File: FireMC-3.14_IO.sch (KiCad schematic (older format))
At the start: 2 parts

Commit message: Schematic Update and Design Calcs for 3V3
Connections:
- net labels removed: +3V3
- wire segments 45 -> 42
- no-connect marks 4 -> 6
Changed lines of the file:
@@
 Connection ~ 2800 2100
-Wire Wire Line
-	2000 2300 1800 2300
-Wire Wire Line
-	1800 2300 1800 1400
-Connection ~ 1800 1500
 Wire Wire Line
 	2000 1900 1900 1900
@@
 	2700 2600 3300 2600
 $Comp
-L GND #PWR?
+L GND #PWR021
 U 1 1 57CB4DBD
 P 1900 3500
-F 0 "#PWR?" H 1900 3250 50  0001 C CNN
+F 0 "#PWR021" H 1900 3250 50  0001 C CNN
 F 1 "GND" H 1900 3350 50  0000 C CNN
 F 2 "" H 1900 3500 50  0000 C CNN
@@
 $EndComp
 $Comp
-L GND #PWR?
+L GND #PWR022
 U 1 1 57CB4DD3
 P 2800 3500
-F 0 "#PWR?" H 2800 3250 50  0001 C CNN
+F 0 "#PWR022" H 2800 3250 50  0001 C CNN
 F 1 "GND" H 2800 3350 50  0000 C CNN
 F 2 "" H 2800 3500 50  0000 C CNN
 F 3 "" H 2800 3500 50  0000 C CNN
 	1    2800 3500
-	1    0    0    -1
-$EndComp
-$Comp
-L +3V3 #PWR?
-U 1 1 57CB4DE9
-P 1800 1400
-F 0 "#PWR?" H 1800 1250 50  0001 C CNN
-F 1 "+3V3" H 1800 1540 50  0000 C CNN
-F 2 "" H 1800 1400 50  0000 C CNN
-F 3 "" H 1800 1400 50  0000 C CNN
-	1    1800 1400
 	1    0    0    -1
 $EndComp
@@
 $EndComp
 $Comp
-L GND #PWR?
+L GND #PWR024
 U 1 1 57CB72B4
 P 4950 1600
-F 0 "#PWR?" H 4950 1350 50  0001 C CNN
+F 0 "#PWR024" H 4950 1350 50  0001 C CNN
 F 1 "GND" H 4950 1450 50  0000 C CNN
 F 2 "" H 4950 1600 50  0000 C CNN
@@
 $EndComp
 $Comp
-L +5F #PWR?
+L +5F #PWR025
 U 1 1 57CB7400
 P 4950 900
-F 0 "#PWR?" H 4950 750 50  0001 C CNN
+F 0 "#PWR025" H 4950 750 50  0001 C CNN
 F 1 "+5F" H 4950 1040 50  0000 C CNN
 F 2 "" H 4950 900 50  0000 C CNN
@@
 $EndComp
 $Comp
-L +5V #PWR?
+L +5V #PWR026
 U 1 1 57CB7418
 P 3850 900
-F 0 "#PWR?" H 3850 750 50  0001 C CNN
+F 0 "#PWR026" H 3850 750 50  0001 C CNN
 F 1 "+5V" H 3850 1040 50  0000 C CNN
 F 2 "" H 3850 900 50  0000 C CNN
@@
 Wire Wire Line
 	4950 1100 5150 1100
-Wire Wire Line
-	1800 1500 2000 1500
 Text GLabel 1400 1600 0    50   Input ~ 0
 SDA1
@@
 Text GLabel 3300 3400 2    50   Input ~ 0
 GPIO21
+NoConn ~ 2000 2300
+NoConn ~ 2000 1500
 $EndSCHEMATC

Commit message: math check
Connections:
- net labels removed: +5F
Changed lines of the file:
@@
 $EndComp
 $Comp
-L +5F #PWR025
-U 1 1 57CB7400
+L +5V #PWR026
+U 1 1 57CB7418
 P 4950 900
-F 0 "#PWR025" H 4950 750 50  0001 C CNN
-F 1 "+5F" H 4950 1040 50  0000 C CNN
+F 0 "#PWR026" H 4950 750 50  0001 C CNN
+F 1 "+5V" H 4950 1040 50  0000 C CNN
 F 2 "" H 4950 900 50  0000 C CNN
 F 3 "" H 4950 900 50  0000 C CNN
@@
 	1    0    0    -1
 $EndComp
-$Comp
-L +5V #PWR026
-U 1 1 57CB7418
-P 3850 900
-F 0 "#PWR026" H 3850 750 50  0001 C CNN
-F 1 "+5V" H 3850 1040 50  0000 C CNN
-F 2 "" H 3850 900 50  0000 C CNN
-F 3 "" H 3850 900 50  0000 C CNN
-	1    3850 900
-	1    0    0    -1
-$EndComp

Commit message: Schematic 80% complete
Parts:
- added J? (x3): Header_1X2, symbol Header_1X2
- added J? (x4): Header_1X3, symbol Header_1X3
- added Q? (x3): Q_PMOS_GDS, symbol Q_PMOS_GDS
- added R? (x2): 3k3, symbol R
- added U?: MCP23S17, symbol MCP23S17
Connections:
- net GND: now also J?.2, J?.2, J?.2, J?.2, Q?.3 (S), Q?.3 (S), Q?.3 (S), U?.10 (VSS), U?.15 (A0), U?.16 (A1), U?.17 (A2)
- net SPI_CE0: now also R?.2, U?.11 (~CS)
- net SPI_MISO: now also U?.14 (SO)
- net SPI_MOSI: now also U?.13 (SI)
- net SPI_SLCK: now also U?.12 (SCK)
- net GPIO12 renamed DIR1
- net GPIO13 renamed DIR2
- net GPIO14 renamed DIR3
- net GPIO15 renamed DIR4
- net GPIO16 renamed STEP1
- net GPIO17 renamed STEP2
- net GPIO18 renamed STEP3
- net GPIO19 renamed STEP4
- net GPIO20 renamed XMAX
- net XMAX: now also J?.3
- net GPIO21 renamed YMAX
- net YMAX: now also J?.3
- net GPIO22 renamed EMAX
- net EMAX: now also J?.3
- new net: J?.2, Q?.2 (D) (x3)
- new net: R?.2, U?.18 (~RST)
- new net AUX: Q?.1 (G), U?.23 (GPA2)
- new net EN1: U?.24 (GPA3)
- new net EN2: U?.25 (GPA4)
- new net EN3: U?.26 (GPA5)
- new net EN4: U?.27 (GPA6)
- new net EXP_INTA: U?.20 (INTA)
- new net EXP_INTB: U?.19 (INTB)
- new net PMP: Q?.1 (G), U?.21 (GPA0)
- new net VCC: J?.1, J?.1, J?.1, J?.1, J?.1, J?.1, J?.1, R?.1, R?.1, U?.9 (VDD)
- new net VLV: Q?.1 (G), U?.22 (GPA1)
- new net ZMAX: J?.3
- no-connect marks 6 -> 15
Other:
- note added: "END STOPS"
- note added: "GPIO EXPANTION\nLOW PRIORITY CONTROL"
- note added: "GPIO12"
- note added: "GPIO13"
- note added: "GPIO14"
- note added: "GPIO15"
- note added: "GPIO16"
- note added: "GPIO17"
- note added: "GPIO18"
- note added: "GPIO19"
- note added: "GPIO20"
- note added: "GPIO21"
- note added: "GPIO22"
- note added: "RASPBERRY PI\nGPIO INTERFACE\nHIGH PRIORITY CONTROL"
- note added: "RASPBERRY PI\nPOWER INTERFACE"
- note added: "SWICTHED DEVICES"
- moved on the sheet: J?

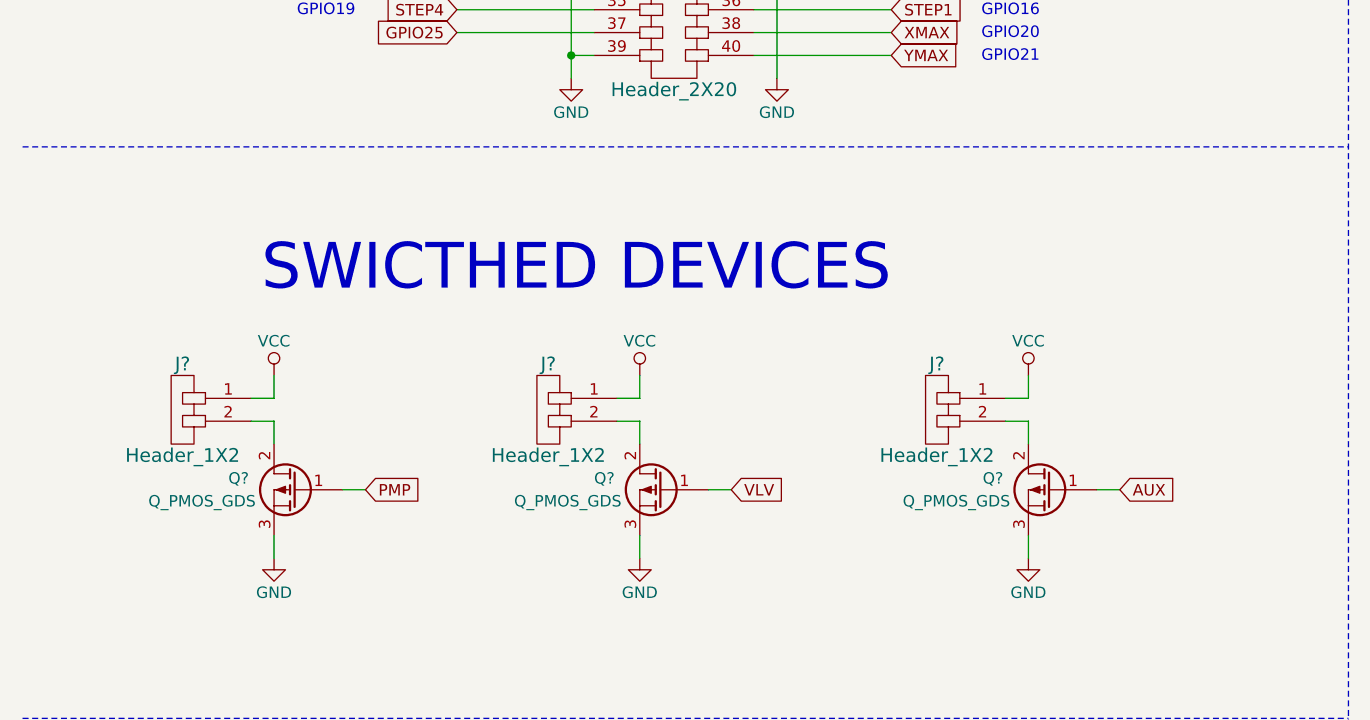
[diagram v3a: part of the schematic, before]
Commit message: Schematic corrections
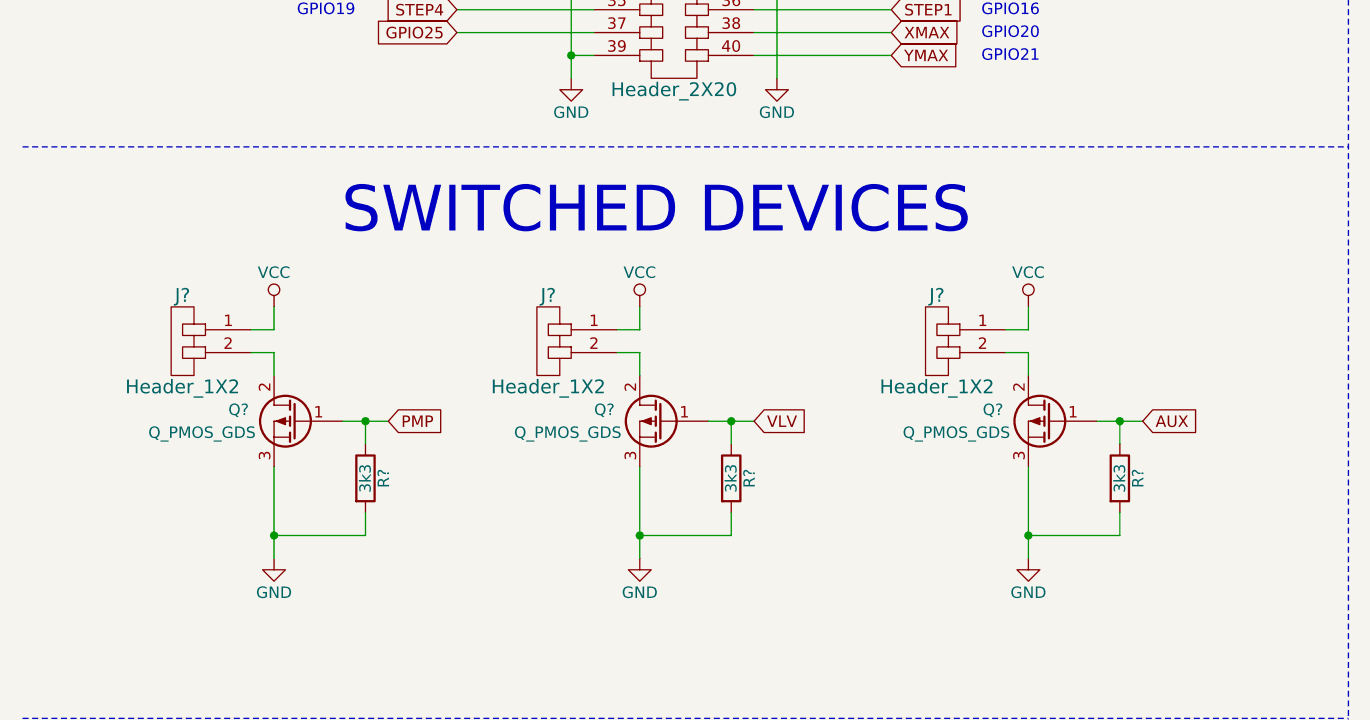
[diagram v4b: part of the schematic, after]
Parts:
- added R? (x3): 3k3, symbol R
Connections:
- net AUX: now also R?.1
- net GND: now also R?.2, R?.2, R?.2
- net PMP: now also R?.1
- net VLV: now also R?.1
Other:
- note added: "SWITCHED DEVICES"
- note removed: "SWICTHED DEVICES"
- moved on the sheet: J?, Q?
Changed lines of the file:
@@
 L Header_1X2 J?
 U 1 1 57D1D48D
-P 1200 5150
-F 0 "J?" H 1200 5350 60  0000 C CNN
-F 1 "Header_1X2" H 1200 4950 60  0000 C CNN
-F 2 "" H 1200 5050 60  0000 C CNN
-F 3 "" H 1200 5050 60  0000 C CNN
-	1    1200 5150
+P 1200 4850
+F 0 "J?" H 1200 5050 60  0000 C CNN
+F 1 "Header_1X2" H 1200 4650 60  0000 C CNN
+F 2 "" H 1200 4750 60  0000 C CNN
+F 3 "" H 1200 4750 60  0000 C CNN
+	1    1200 4850
 	-1   0    0    -1
 $EndComp
@@
 L Header_1X2 J?
 U 1 1 57D1D4C7
-P 2800 5150
-F 0 "J?" H 2800 5350 60  0000 C CNN
-F 1 "Header_1X2" H 2800 4950 60  0000 C CNN
-F 2 "" H 2800 5050 60  0000 C CNN
-F 3 "" H 2800 5050 60  0000 C CNN
-	1    2800 5150
+P 2800 4850
+F 0 "J?" H 2800 5050 60  0000 C CNN
+F 1 "Header_1X2" H 2800 4650 60  0000 C CNN
+F 2 "" H 2800 4750 60  0000 C CNN
+F 3 "" H 2800 4750 60  0000 C CNN
+	1    2800 4850
 	-1   0    0    -1
 $EndComp
@@
 L Header_1X2 J?
 U 1 1 57D1D4FC
-P 4500 5150
-F 0 "J?" H 4500 5350 60  0000 C CNN
-F 1 "Header_1X2" H 4500 4950 60  0000 C CNN
-F 2 "" H 4500 5050 60  0000 C CNN
-F 3 "" H 4500 5050 60  0000 C CNN
-	1    4500 5150
+P 4500 4850
+F 0 "J?" H 4500 5050 60  0000 C CNN
+F 1 "Header_1X2" H 4500 4650 60  0000 C CNN
+F 2 "" H 4500 4750 60  0000 C CNN
+F 3 "" H 4500 4750 60  0000 C CNN
+	1    4500 4850
 	-1   0    0    -1
 $EndComp
@@
 L VCC #PWR?
 U 1 1 57D1D660
-P 4900 5000
-F 0 "#PWR?" H 4900 4850 50  0001 C CNN
-F 1 "VCC" H 4900 5150 50  0000 C CNN
-F 2 "" H 4900 5000 50  0000 C CNN
-F 3 "" H 4900 5000 50  0000 C CNN
-	1    4900 5000
+P 4900 4700
+F 0 "#PWR?" H 4900 4550 50  0001 C CNN
+F 1 "VCC" H 4900 4850 50  0000 C CNN
+F 2 "" H 4900 4700 50  0000 C CNN
+F 3 "" H 4900 4700 50  0000 C CNN
+	1    4900 4700
 	1    0    0    -1
 $EndComp
@@
 L VCC #PWR?
 U 1 1 57D1DEDE
-P 3200 5000
-F 0 "#PWR?" H 3200 4850 50  0001 C CNN
-F 1 "VCC" H 3200 5150 50  0000 C CNN
-F 2 "" H 3200 5000 50  0000 C CNN
-F 3 "" H 3200 5000 50  0000 C CNN
-	1    3200 5000
+P 3200 4700
+F 0 "#PWR?" H 3200 4550 50  0001 C CNN
+F 1 "VCC" H 3200 4850 50  0000 C CNN
+F 2 "" H 3200 4700 50  0000 C CNN
+F 3 "" H 3200 4700 50  0000 C CNN
+	1    3200 4700
 	1    0    0    -1
 $EndComp
@@
 L VCC #PWR?
 U 1 1 57D1DF07
-P 1600 5000
-F 0 "#PWR?" H 1600 4850 50  0001 C CNN
-F 1 "VCC" H 1600 5150 50  0000 C CNN
-F 2 "" H 1600 5000 50  0000 C CNN
-F 3 "" H 1600 5000 50  0000 C CNN
-	1    1600 5000
+P 1600 4700
+F 0 "#PWR?" H 1600 4550 50  0001 C CNN
+F 1 "VCC" H 1600 4850 50  0000 C CNN
+F 2 "" H 1600 4700 50  0000 C CNN
+F 3 "" H 1600 4700 50  0000 C CNN
+	1    1600 4700
 	1    0    0    -1
 $EndComp
@@
 L Q_PMOS_GDS Q?
 U 1 1 57D53BF1
-P 1700 5500
-F 0 "Q?" H 2000 5550 50  0000 R CNN
-F 1 "Q_PMOS_GDS" H 2350 5450 50  0000 R CNN
-F 2 "" H 1900 5600 50  0000 C CNN
-F 3 "" H 1700 5500 50  0000 C CNN
-	1    1700 5500
+P 1700 5200
+F 0 "Q?" H 2000 5250 50  0000 R CNN
+F 1 "Q_PMOS_GDS" H 2350 5150 50  0000 R CNN
+F 2 "" H 1900 5300 50  0000 C CNN
+F 3 "" H 1700 5200 50  0000 C CNN
+	1    1700 5200
 	-1   0    0    -1
 $EndComp
@@
 L Q_PMOS_GDS Q?
 U 1 1 57D53C27
-P 3300 5500
-F 0 "Q?" H 3600 5550 50  0000 R CNN
-F 1 "Q_PMOS_GDS" H 3950 5450 50  0000 R CNN
-F 2 "" H 3500 5600 50  0000 C CNN
-F 3 "" H 3300 5500 50  0000 C CNN
-	1    3300 5500
+P 3300 5200
+F 0 "Q?" H 3600 5250 50  0000 R CNN
+F 1 "Q_PMOS_GDS" H 3950 5150 50  0000 R CNN
+F 2 "" H 3500 5300 50  0000 C CNN
+F 3 "" H 3300 5200 50  0000 C CNN
+	1    3300 5200
 	-1   0    0    -1
 $EndComp
@@
 L Q_PMOS_GDS Q?
 U 1 1 57D53C75
-P 5000 5500
-F 0 "Q?" H 5300 5550 50  0000 R CNN
-F 1 "Q_PMOS_GDS" H 5650 5450 50  0000 R CNN
-F 2 "" H 5200 5600 50  0000 C CNN
-F 3 "" H 5000 5500 50  0000 C CNN
-	1    5000 5500
-	-1   0    0    -1
-$EndComp
-Text GLabel 2000 5500 2    50   Input ~ 0
+P 5000 5200
+F 0 "Q?" H 5300 5250 50  0000 R CNN
+F 1 "Q_PMOS_GDS" H 5650 5150 50  0000 R CNN
+F 2 "" H 5200 5300 50  0000 C CNN
+F 3 "" H 5000 5200 50  0000 C CNN
+	1    5000 5200
+	-1   0    0    -1
+$EndComp
+Text GLabel 2100 5200 2    50   Input ~ 0
 PMP
-Text GLabel 3600 5500 2    50   Input ~ 0
+Text GLabel 3700 5200 2    50   Input ~ 0
 VLV
-Text GLabel 5300 5500 2    50   Input ~ 0
+Text GLabel 5400 5200 2    50   Input ~ 0
 AUX
 Wire Wire Line
-	1600 5300 1600 5200
-Wire Wire Line
-	1600 5200 1500 5200
-Wire Wire Line
-	1500 5100 1600 5100
-Wire Wire Line
-	1600 5100 1600 5000
-Wire Wire Line
-	1600 5800 1600 5700
-Wire Wire Line
-	1900 5500 2000 5500
-Wire Wire Line
-	3100 5200 3200 5200
-Wire Wire Line
-	3200 5200 3200 5300
-Wire Wire Line
-	3100 5100 3200 5100
-Wire Wire Line
-	3200 5100 3200 5000
-Wire Wire Line
-	3500 5500 3600 5500
-Wire Wire Line
-	3200 5800 3200 5700
-Wire Wire Line
-	4800 5100 4900 5100
-Wire Wire Line
-	4900 5100 4900 5000
-Wire Wire Line
-	4800 5200 4900 5200
-Wire Wire Line
-	4900 5200 4900 5300
-Wire Wire Line
-	5200 5500 5300 5500
-Wire Wire Line
-	4900 5800 4900 5700
+	1600 5000 1600 4900
+Wire Wire Line
+	1600 4900 1500 4900
+Wire Wire Line
+	1500 4800 1600 4800
+Wire Wire Line
+	1600 4800 1600 4700
+Wire Wire Line
+	1600 5400 1600 5800
+Wire Wire Line
+	1900 5200 2100 5200
+Wire Wire Line
+	3100 4900 3200 4900
+Wire Wire Line
+	3200 4900 3200 5000
+Wire Wire Line
+	3100 4800 3200 4800
+Wire Wire Line
+	3200 4800 3200 4700
+Wire Wire Line
+	3500 5200 3700 5200
+Wire Wire Line
+	3200 5400 3200 5800
+Wire Wire Line
+	4800 4800 4900 4800
+Wire Wire Line
+	4900 4800 4900 4700
+Wire Wire Line
+	4800 4900 4900 4900
+Wire Wire Line
+	4900 4900 4900 5000
+Wire Wire Line
+	5200 5200 5400 5200
+Wire Wire Line
+	4900 5400 4900 5800
 Wire Wire Line
 	8400 4600 8300 4600
@@
 Text Notes 10300 3650 2    200  ~ 0
 GPIO EXPANTION\nLOW PRIORITY CONTROL
-Text Notes 4300 4650 2    200  ~ 0
-SWICTHED DEVICES
+Text Notes 4650 4400 2    200  ~ 0
+SWITCHED DEVICES
 Text Notes 3750 6900 2    200  ~ 0
 END STOPS
@@
 NoConn ~ 9400 5900
 NoConn ~ 9400 6000
+$Comp
+L R R?
+U 1 1 57D58CCB
+P 5300 5450
+F 0 "R?" V 5380 5450 50  0000 C CNN
+F 1 "3k3" V 5300 5450 50  0000 C CNN
+F 2 "" V 5230 5450 50  0000 C CNN
+F 3 "" H 5300 5450 50  0000 C CNN
+	1    5300 5450
+	1    0    0    -1
+$EndComp
+$Comp
+L R R?
+U 1 1 57D58E2F
+P 3600 5450
+F 0 "R?" V 3680 5450 50  0000 C CNN
+F 1 "3k3" V 3600 5450 50  0000 C CNN
+F 2 "" V 3530 5450 50  0000 C CNN
+F 3 "" H 3600 5450 50  0000 C CNN
+	1    3600 5450
+	1    0    0    -1
+$EndComp
+$Comp
+L R R?
+U 1 1 57D58EA6
+P 2000 5450
+F 0 "R?" V 2080 5450 50  0000 C CNN
+F 1 "3k3" V 2000 5450 50  0000 C CNN
+F 2 "" V 1930 5450 50  0000 C CNN
+F 3 "" H 2000 5450 50  0000 C CNN
+	1    2000 5450
+	1    0    0    -1
+$EndComp
+Wire Wire Line
+	5300 5300 5300 5200
+Connection ~ 5300 5200
+Wire Wire Line
+	5300 5600 5300 5700
+Wire Wire Line
+	5300 5700 4900 5700
+Connection ~ 4900 5700
+Wire Wire Line
+	3200 5700 3600 5700
+Wire Wire Line
+	3600 5700 3600 5600
+Connection ~ 3200 5700
+Wire Wire Line
+	2000 5600 2000 5700
+Wire Wire Line
+	2000 5700 1600 5700
+Connection ~ 1600 5700
+Wire Wire Line
+	2000 5200 2000 5300
+Connection ~ 2000 5200
+Wire Wire Line
+	3600 5200 3600 5300
+Connection ~ 3600 5200
 $EndSCHEMATC

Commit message: Schematic Complete for full comments
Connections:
- net GPIO4 renamed ~ALLSTOP
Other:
- note added: "GPIO EXPANSION\nLOW PRIORITY CONTROL"
- note added: "GPIO4"
- note removed: "GPIO EXPANTION\nLOW PRIORITY CONTROL"
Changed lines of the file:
@@
 SCL1
 Text GLabel 2400 2000 0    50   Input ~ 0
-GPIO4
+~ALLSTOP
 Text GLabel 2400 2200 0    50   Input ~ 0
 STEP2
@@
 RASPBERRY PI\nPOWER INTERFACE
 Text Notes 10300 3650 2    200  ~ 0
-GPIO EXPANTION\nLOW PRIORITY CONTROL
+GPIO EXPANSION\nLOW PRIORITY CONTROL
 Text Notes 4650 4400 2    200  ~ 0
 SWITCHED DEVICES
@@
 	3600 5200 3600 5300
 Connection ~ 3600 5200
+Text Notes 1700 2040 0    50   ~ 0
+GPIO4
 $EndSCHEMATC

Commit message: PCB Layout experimentation
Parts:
- J12, J14, J16, J18: renamed from J?; footprint (none) -> IPC_MFG:SULLINS_PRPC003SAAN-RC
- J13, J15, J19: renamed from J?; footprint (none) -> IPC_MFG:SULLINS_PRPC002SAAN-RC
- J17: renamed from J?; footprint (none) -> IPC_MFG:SULLINS_PPTC202LFBN-RC
- J20: renamed from J?; footprint (none) -> IPC_MFG:MOLEX_22-23-2041
- Q5, Q6, Q7: renamed from Q?; value Q_PMOS_GDS -> STD86N3LH5; footprint (none) -> IPC_TO:TO228P972X240-3N; symbol Q_PMOS_GDS -> Q_NMOS_GDS
- R29, R30, R31, R32, R33: renamed from R?; footprint (none) -> IPC_RES:RESC1608X55N
- U9: renamed from U?; footprint (none) -> IPC_SOIC127P:SOIC127P1030X265-28N
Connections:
- net GPIO23 is gone; now on net EMAX: J17.16
- net EMAX: no longer J17.15
- net ZMAX: now also J17.15
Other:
- note added: "GPIO23"

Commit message: Time to Update.  Board layout started.
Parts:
- J17: footprint IPC_MFG:SULLINS_PPTC202LFBN-RC -> IPC_MFG:SULLINS_PPxC202LFBN-RC; Contact Finish (none) -> Gold (P); Mfg PN (none) -> PPPC200LFBN-RC
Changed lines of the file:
@@
 LIBS:Maxim Integrated
 LIBS:Intersil
+LIBS:mounting hole
 LIBS:FireMC-3.14-cache
 EELAYER 25 0
@@
 F 0 "J17" H 3350 3750 60  0000 C CNN
 F 1 "Header_2X20" H 3350 1550 60  0000 C CNN
-F 2 "IPC_MFG:SULLINS_PPTC202LFBN-RC" H 3350 2650 60  0001 C CNN
+F 2 "IPC_MFG:SULLINS_PPxC202LFBN-RC" H 3350 2650 60  0001 C CNN
 F 3 "" H 3350 2650 60  0000 C CNN
+F 4 "PPPC200LFBN-RC" H 3350 2650 60  0001 C CNN "Mfg PN"
+F 5 "Gold (P)" H 3350 2650 60  0001 C CNN "Contact Finish"
 	1    3350 2650
 	1    0    0    -1
@@
 	3700 2800 4300 2800
 $Comp
-L GND #PWR025
+L GND #PWR08
 U 1 1 57CB4DBD
 P 2900 3700
-F 0 "#PWR025" H 2900 3450 50  0001 C CNN
+F 0 "#PWR08" H 2900 3450 50  0001 C CNN
 F 1 "GND" H 2900 3550 50  0000 C CNN
 F 2 "" H 2900 3700 50  0000 C CNN
@@
 $EndComp
 $Comp
-L GND #PWR026
+L GND #PWR09
 U 1 1 57CB4DD3
 P 3800 3700
-F 0 "#PWR026" H 3800 3450 50  0001 C CNN
+F 0 "#PWR09" H 3800 3450 50  0001 C CNN
 F 1 "GND" H 3800 3550 50  0000 C CNN
 F 2 "" H 3800 3700 50  0000 C CNN
@@
 $EndComp
 $Comp
-L GND #PWR027
+L GND #PWR010
 U 1 1 57CB72B4
 P 8400 2100
-F 0 "#PWR027" H 8400 1850 50  0001 C CNN
+F 0 "#PWR010" H 8400 1850 50  0001 C CNN
 F 1 "GND" H 8400 1950 50  0000 C CNN
 F 2 "" H 8400 2100 50  0000 C CNN
@@
 $EndComp
 $Comp
-L +5V #PWR028
+L +5V #PWR011
 U 1 1 57CB7418
 P 8400 1600
-F 0 "#PWR028" H 8400 1450 50  0001 C CNN
+F 0 "#PWR011" H 8400 1450 50  0001 C CNN
 F 1 "+5V" H 8400 1740 50  0000 C CNN
 F 2 "" H 8400 1600 50  0000 C CNN
@@
 $EndComp
 $Comp
-L VCC #PWR029
+L VCC #PWR012
 U 1 1 57D1D60D
 P 1300 7250
-F 0 "#PWR029" H 1300 7100 50  0001 C CNN
+F 0 "#PWR012" H 1300 7100 50  0001 C CNN
 F 1 "VCC" H 1300 7400 50  0000 C CNN
 F 2 "" H 1300 7250 50  0000 C CNN
@@
 $EndComp
 $Comp
-L VCC #PWR030
+L VCC #PWR013
 U 1 1 57D1D63A
 P 3500 7250
-F 0 "#PWR030" H 3500 7100 50  0001 C CNN
+F 0 "#PWR013" H 3500 7100 50  0001 C CNN
 F 1 "VCC" H 3500 7400 50  0000 C CNN
 F 2 "" H 3500 7250 50  0000 C CNN
@@
 $EndComp
 $Comp
-L VCC #PWR031
+L VCC #PWR014
 U 1 1 57D1D660
 P 4900 4700
-F 0 "#PWR031" H 4900 4550 50  0001 C CNN
+F 0 "#PWR014" H 4900 4550 50  0001 C CNN
 F 1 "VCC" H 4900 4850 50  0000 C CNN
 F 2 "" H 4900 4700 50  0000 C CNN
@@
 $EndComp
 $Comp
-L VCC #PWR032
+L VCC #PWR015
 U 1 1 57D1D686
 P 4600 7250
-F 0 "#PWR032" H 4600 7100 50  0001 C CNN
+F 0 "#PWR015" H 4600 7100 50  0001 C CNN
 F 1 "VCC" H 4600 7400 50  0000 C CNN
 F 2 "" H 4600 7250 50  0000 C CNN
@@
 $EndComp
 $Comp
-L GND #PWR033
+L GND #PWR016
 U 1 1 57D1D6AC
 P 1300 7650
-F 0 "#PWR033" H 1300 7400 50  0001 C CNN
+F 0 "#PWR016" H 1300 7400 50  0001 C CNN
 F 1 "GND" H 1300 7500 50  0000 C CNN
 F 2 "" H 1300 7650 50  0000 C CNN
@@
 $EndComp
 $Comp
-L GND #PWR034
+L GND #PWR017
 U 1 1 57D1D6D2
 P 1600 5800
-F 0 "#PWR034" H 1600 5550 50  0001 C CNN
+F 0 "#PWR017" H 1600 5550 50  0001 C CNN
 F 1 "GND" H 1600 5650 50  0000 C CNN
 F 2 "" H 1600 5800 50  0000 C CNN
@@
 $EndComp
 $Comp
-L GND #PWR035
+L GND #PWR018
 U 1 1 57D1D6F8
 P 3200 5800
-F 0 "#PWR035" H 3200 5550 50  0001 C CNN
+F 0 "#PWR018" H 3200 5550 50  0001 C CNN
 F 1 "GND" H 3200 5650 50  0000 C CNN
 F 2 "" H 3200 5800 50  0000 C CNN
@@
 $EndComp
 $Comp
-L GND #PWR036
+L GND #PWR019
 U 1 1 57D1D71E
 P 4900 5800
-F 0 "#PWR036" H 4900 5550 50  0001 C CNN
+F 0 "#PWR019" H 4900 5550 50  0001 C CNN
 F 1 "GND" H 4900 5650 50  0000 C CNN
 F 2 "" H 4900 5800 50  0000 C CNN
@@
 $EndComp
 $Comp
-L GND #PWR037
+L GND #PWR020
 U 1 1 57D1D744
 P 4600 7650
-F 0 "#PWR037" H 4600 7400 50  0001 C CNN
+F 0 "#PWR020" H 4600 7400 50  0001 C CNN
 F 1 "GND" H 4600 7500 50  0000 C CNN
 F 2 "" H 4600 7650 50  0000 C CNN
@@
 $EndComp
 $Comp
-L VCC #PWR038
+L VCC #PWR021
 U 1 1 57D1D96E
 P 7700 4300
-F 0 "#PWR038" H 7700 4150 50  0001 C CNN
+F 0 "#PWR021" H 7700 4150 50  0001 C CNN
 F 1 "VCC" H 7700 4450 50  0000 C CNN
 F 2 "" H 7700 4300 50  0000 C CNN
@@
 $EndComp
 $Comp
-L GND #PWR039
+L GND #PWR022
 U 1 1 57D1D997
 P 8300 6100
-F 0 "#PWR039" H 8300 5850 50  0001 C CNN
+F 0 "#PWR022" H 8300 5850 50  0001 C CNN
 F 1 "GND" H 8300 5950 50  0000 C CNN
 F 2 "" H 8300 6100 50  0000 C CNN
@@
 	1300 7350 1300 7250
 $Comp
-L VCC #PWR040
+L VCC #PWR023
 U 1 1 57D1DEB5
 P 2400 7250
-F 0 "#PWR040" H 2400 7100 50  0001 C CNN
+F 0 "#PWR023" H 2400 7100 50  0001 C CNN
 F 1 "VCC" H 2400 7400 50  0000 C CNN
 F 2 "" H 2400 7250 50  0000 C CNN
@@
 $EndComp
 $Comp
-L VCC #PWR041
+L VCC #PWR024
 U 1 1 57D1DEDE
 P 3200 4700
-F 0 "#PWR041" H 3200 4550 50  0001 C CNN
+F 0 "#PWR024" H 3200 4550 50  0001 C CNN
 F 1 "VCC" H 3200 4850 50  0000 C CNN
 F 2 "" H 3200 4700 50  0000 C CNN
@@
 $EndComp
 $Comp
-L VCC #PWR042
+L VCC #PWR025
 U 1 1 57D1DF07
 P 1600 4700
-F 0 "#PWR042" H 1600 4550 50  0001 C CNN
+F 0 "#PWR025" H 1600 4550 50  0001 C CNN
 F 1 "VCC" H 1600 4850 50  0000 C CNN
 F 2 "" H 1600 4700 50  0000 C CNN
@@
 $EndComp
 $Comp
-L GND #PWR043
+L GND #PWR026
 U 1 1 57D1DF30
 P 3500 7650
-F 0 "#PWR043" H 3500 7400 50  0001 C CNN
+F 0 "#PWR026" H 3500 7400 50  0001 C CNN
 F 1 "GND" H 3500 7500 50  0000 C CNN
 F 2 "" H 3500 7650 50  0000 C CNN
@@
 $EndComp
 $Comp
-L GND #PWR044
+L GND #PWR027
 U 1 1 57D1DF59
 P 2400 7650
-F 0 "#PWR044" H 2400 7400 50  0001 C CNN
+F 0 "#PWR027" H 2400 7400 50  0001 C CNN
 F 1 "GND" H 2400 7500 50  0000 C CNN
 F 2 "" H 2400 7650 50  0000 C CNN
